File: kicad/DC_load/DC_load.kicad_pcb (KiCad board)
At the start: 2 copper layers, 110 x 145 mm, 190 parts, among them J1 BNC, J10 DC fan connector, J2 red_terminal, J3 red terminal, J4 black terminal, J5 black terminal, J6 USB_B, J8 FT232 programming port, J9 Conn_01x04_Socket, Q1 MMBT5401, Q13 AO3400A, Q3 FQP19N20C, Q4 FQP19N20C, Q5 FQP19N20C, Q6 FQP19N20C, SW1 RotaryEncoder_Switch, SW2 RotaryEncoder_Switch, SW3 SW_Push, SW8 SW_Push, U1 FSA3157P6X, U10 FSA3157P6X, U11 FSA3157P6X, U12 FSA3157P6X, U13 TLV9062, U14 AMS1117-3.3, U15 74HC14D653, U16 93LCxxB, U17 CH340C, U18 TL431DBZ, U2 Screen, U3 NCS21802, U4 NCS21802, U5 TLV9062, U6 TLV9062, U7 LMT84LPM, U8 STM32F103C8Tx, U9 Front plate

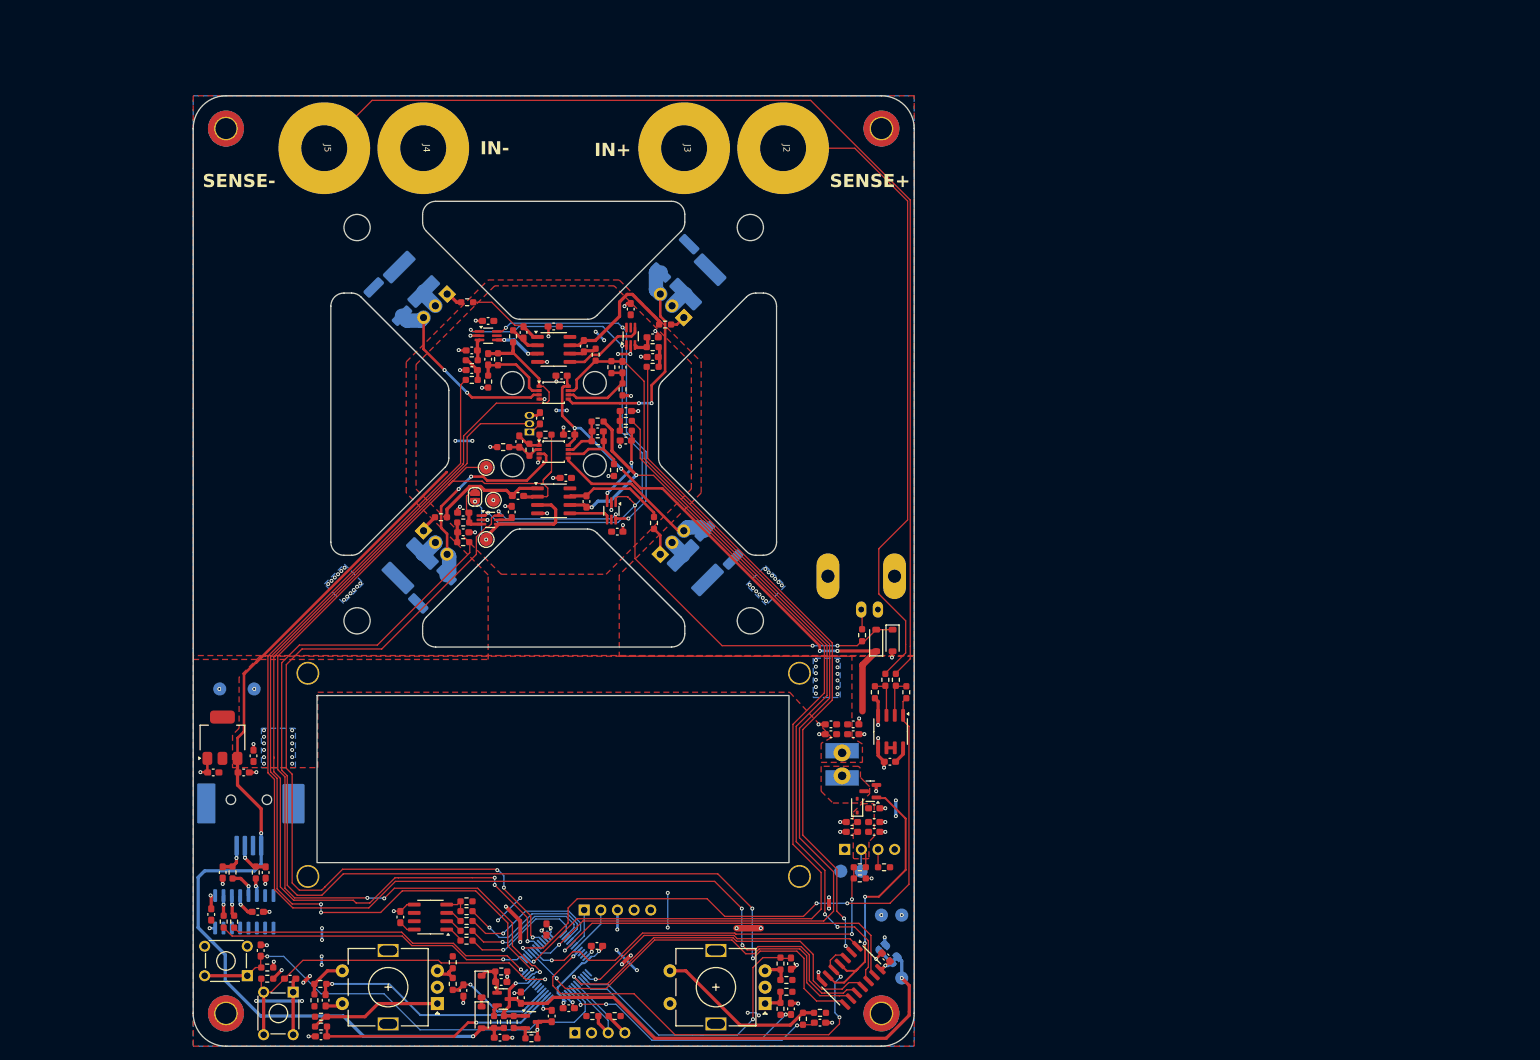
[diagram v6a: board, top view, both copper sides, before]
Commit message: Vbe multiplier, constant current source 12V mosfet gate driver. RC filters moved lower. INA181 for 20x gain, 50 mOhm shunts. Jumper moved to BNC. Rough placement initiated.
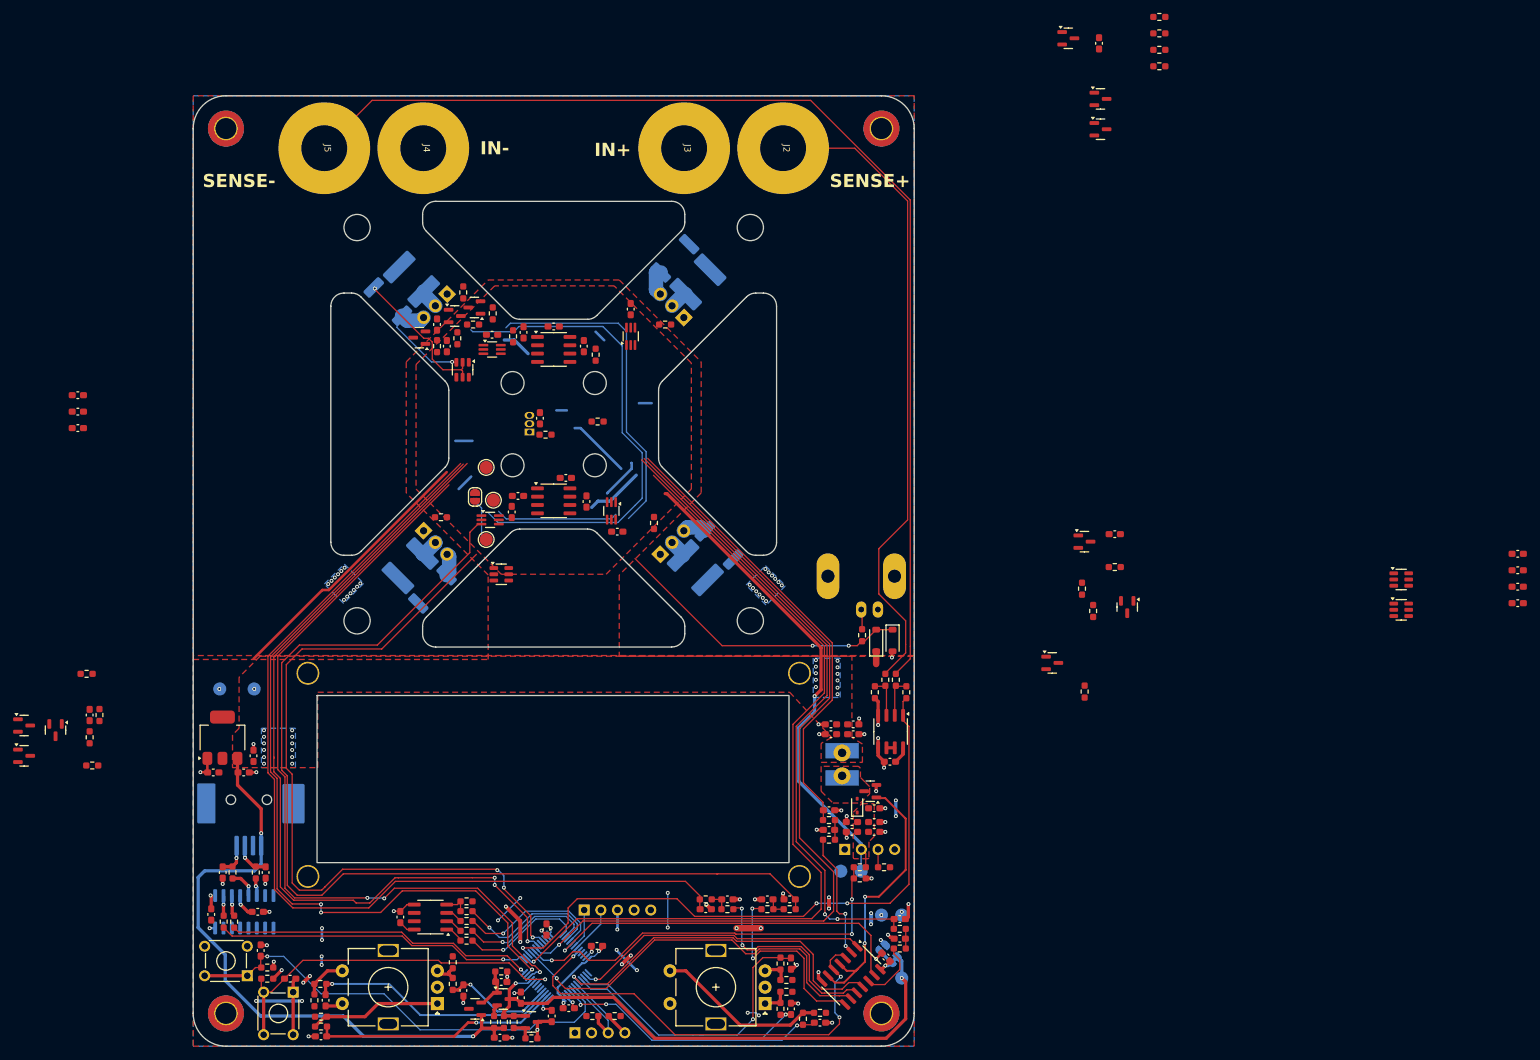
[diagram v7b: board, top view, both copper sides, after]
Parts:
- removed U3, U4: NCS21802, Package_SO:OnSemi_Micro8
- added C64: 100n, Capacitor_SMD:C_0603_1608Metric_Pad1.08x0.95mm_HandSolder, F.Cu at (252.1, 124.9)
- added C65: 100n, Capacitor_SMD:C_0603_1608Metric_Pad1.08x0.95mm_HandSolder, F.Cu at (252.1, 127.4)
- added C66: 100n, Capacitor_SMD:C_0603_1608Metric_Pad1.08x0.95mm_HandSolder, F.Cu at (88.7, 88.2)
- added C67: 100n, Capacitor_SMD:C_0603_1608Metric_Pad1.08x0.95mm_HandSolder, F.Cu at (32.4, 95.7)
- added C68: 100n, Capacitor_SMD:C_0603_1608Metric_Pad1.08x0.95mm_HandSolder, F.Cu at (32.4, 98.2)
- added C69: 100n, Capacitor_SMD:C_0603_1608Metric_Pad1.08x0.95mm_HandSolder, F.Cu at (32.4, 100.7)
- added D6: BAV99, Package_TO_SOT_SMD:SOT-23, F.Cu at (93.0, 189.3)
- added D7: BAV99, Package_TO_SOT_SMD:SOT-23, F.Cu at (84.5, 86.9)
- added D8: BAV99, Package_TO_SOT_SMD:SOT-23, F.Cu at (183.5, 41.2)
- added Q10: MMBT5401, Package_TO_SOT_SMD:SOT-23, F.Cu at (89.9, 83.6)
- added Q11: MMBT5551L, Package_TO_SOT_SMD:SOT-23, F.Cu at (92.9, 82.3)
- added Q12: MMBT5401, Package_TO_SOT_SMD:SOT-23, F.Cu at (188.4, 50.5)
- added Q14: MMBT5551L, Package_TO_SOT_SMD:SOT-23, F.Cu at (188.4, 55.1)
- added Q2: MMBT5401, Package_TO_SOT_SMD:SOT-23, F.Cu at (24.2, 146.1)
- added Q7: MMBT5551L, Package_TO_SOT_SMD:SOT-23, F.Cu at (24.2, 150.7)
- added Q8: MMBT5401, Package_TO_SOT_SMD:SOT-23, F.Cu at (181.1, 136.5)
- added Q9: MMBT5551L, Package_TO_SOT_SMD:SOT-23, F.Cu at (186.0, 118.0)
- added R67: 10k, Resistor_SMD:R_0603_1608Metric_Pad0.98x0.95mm_HandSolder, F.Cu at (87.2, 88.2)
- added R68: 10k, Resistor_SMD:R_0603_1608Metric_Pad0.98x0.95mm_HandSolder, F.Cu at (92.7, 84.9)
- added R69: 3k3, Resistor_SMD:R_0603_1608Metric_Pad0.98x0.95mm_HandSolder, F.Cu at (95.7, 83.2)
- added R70: 100, Resistor_SMD:R_0603_1608Metric_Pad0.98x0.95mm_HandSolder, F.Cu at (90.3, 87.0)
- added R71: 100, Resistor_SMD:R_0603_1608Metric_Pad0.98x0.95mm_HandSolder, F.Cu at (197.4, 38.0)
- added R72: 10k, Resistor_SMD:R_0603_1608Metric_Pad0.98x0.95mm_HandSolder, F.Cu at (197.4, 40.5)
- added R73: 3k3, Resistor_SMD:R_0603_1608Metric_Pad0.98x0.95mm_HandSolder, F.Cu at (197.4, 43.0)
- added R74: 10k, Resistor_SMD:R_0603_1608Metric_Pad0.98x0.95mm_HandSolder, F.Cu at (197.4, 45.5)
- added U19: INA181, Package_TO_SOT_SMD:SOT-23-6, F.Cu at (97.0, 123.0)
- added U20: INA181, Package_TO_SOT_SMD:SOT-23-6, F.Cu at (91.1, 91.8)
- added U21: INA181, Package_TO_SOT_SMD:SOT-23-6, F.Cu at (234.3, 123.8)
- added U22: INA181, Package_TO_SOT_SMD:SOT-23-6, F.Cu at (234.3, 128.4)
- C1, C2, C4, C7: value 100p -> 10u
- D3, D4: value 1N4148W -> BAV99; footprint Diode_SMD:D_SOD-123 -> Package_TO_SOT_SMD:SOT-23
- R1, R13, R16, R8: value 100 -> 10k
- R11, R18: value 10k -> 3k3
- R14, R15, R3, R9: value 10 mOhm -> 50 mOhm
- R31, R6: value 10k -> 100
- moved C46 148.9 mm to (252.1, 122.4)
- moved C9 145.9 mm to (252.1, 119.9)
- moved D4 116.7 mm to (192.5, 128.0)
- moved C24 92.4 mm to (128.2, 174.1), turned to 180 degrees
- moved C1 91.9 mm to (190.6, 116.9), turned to 0 degrees
- moved R11 91.6 mm to (34.6, 152.2)
- moved R31 91.1 mm to (190.6, 121.9), turned to 0 degrees
- moved C25 90.7 mm to (157.8, 178.6), turned to 180 degrees
- moved R25 90.7 mm to (157.8, 180.1), turned to 180 degrees
- moved C23 89.7 mm to (131.5, 172.6), turned to 0 degrees
- moved R23 89.7 mm to (131.5, 174.1), turned to 0 degrees
- moved R24 89.7 mm to (128.2, 172.6), turned to 0 degrees
- moved C7 87.9 mm to (188.2, 42.0)
- moved R26 86.7 mm to (157.8, 177.1), turned to 0 degrees
- moved C26 84.1 mm to (157.8, 175.6), turned to 180 degrees
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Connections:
- C1 pad 1: Net-(C1-Pad1) -> 12V
- C1 pad 2: Net-(U3A--) -> Net-(D4-A)
- C10 pad 2: 5V -> 3V3
- C11 pad 2: 5V -> 3V3
- C2 pad 1: /Microcontroller/CH2_MEAS -> 12V
- C2 pad 2: Net-(U4A--) -> Net-(D3-A)
- C20 pad 1: /Microcontroller/CH1_MEAS -> Net-(U5A--)
- C20 pad 2: Net-(C20-Pad2) -> Net-(Q7-E)
- C22 pad 2: Net-(JP3-A) -> Net-(C22-Pad2)
- C3 pad 2: Net-(C3-Pad2) -> Net-(Q11-E)
- C35 pad 1: Net-(D3-K) -> Net-(D6-A)
- C4 pad 1: Net-(C4-Pad1) -> 12V
- C4 pad 2: Net-(U3B--) -> Net-(D7-A)
- C5 pad 1: /Microcontroller/CH3_MEAS -> Net-(U5B--)
- C5 pad 2: Net-(C5-Pad2) -> Net-(Q9-E)
- C54 pad 1: /Microcontroller/FAN_OUT -> 12V
- C55 pad 1: /Microcontroller/FAN_OUT -> 12V
- C6 pad 2: Net-(C6-Pad2) -> Net-(Q14-E)
- C61 pad 1: /Microcontroller/FAN_OUT -> 12V
- C62 pad 1: /Microcontroller/FAN_OUT -> 12V
- C63 pad 1: /Microcontroller/FAN_OUT -> 12V
- C7 pad 1: /Microcontroller/CH4_MEAS -> 12V
- C7 pad 2: Net-(U4B--) -> Net-(D8-A)
- C8 pad 1: 5V -> 3V3
- D3 pad 1: Net-(D3-K) -> 12V
- D4 pad 1: Net-(D3-A) -> 12V
- D4 pad 2: 5V -> Net-(D4-A)
- D5 pad 1: /Microcontroller/FAN_OUT -> 12V
- J10 pad 2: /Microcontroller/FAN_OUT -> 12V
- J10 pad 4: unconnected-(J10-Pin_4-Pad4) -> FAN_PWM
- JP3 pad 1: Net-(JP3-A) -> /Microcontroller/BNC_CONTROL
- Q1 pad 1: Net-(D3-K) -> Net-(D6-A)
- R1 pad 1: GND -> Net-(D3-A)
- R1 pad 2: Net-(U3A--) -> GND
- R10 pad 1: Net-(C4-Pad1) -> /Microcontroller/CH3_MEAS
- R10 pad 2: /Microcontroller/CH3_MEAS -> Net-(U5B--)
- R11 pad 1: Net-(U3B--) -> Net-(Q7-B)
- R11 pad 2: Net-(C4-Pad1) -> Net-(Q7-E)
- R12 pad 2: Net-(C5-Pad2) -> Net-(Q8-C)
- R13 pad 1: GND -> Net-(D4-A)
- R13 pad 2: Net-(U3B--) -> GND
- R16 pad 1: GND -> Net-(Q8-C)
- R16 pad 2: Net-(U4B--) -> Net-(Q9-B)
- R17 pad 2: Net-(C6-Pad2) -> Net-(Q12-C)
- R18 pad 1: Net-(U4B--) -> Net-(Q9-B)
- R18 pad 2: /Microcontroller/CH4_MEAS -> Net-(Q9-E)
- R2 pad 2: Net-(C20-Pad2) -> Net-(Q2-C)
- R21 pad 1: Net-(JP3-A) -> Net-(C22-Pad2)
- R31 pad 1: Net-(U3A--) -> Net-(Q8-E)
- R31 pad 2: Net-(C1-Pad1) -> 12V
- R4 pad 1: Net-(C1-Pad1) -> /Microcontroller/CH1_MEAS
- R4 pad 2: /Microcontroller/CH1_MEAS -> Net-(U5A--)
- R58 pad 1: Net-(D3-K) -> Net-(D6-A)
- R6 pad 1: Net-(U4A--) -> Net-(Q2-E)
- R6 pad 2: /Microcontroller/CH2_MEAS -> 12V
- R66 pad 1: /Microcontroller/FAN_OUT -> 12V
- R7 pad 2: Net-(C3-Pad2) -> Net-(Q10-C)
- R8 pad 1: GND -> Net-(Q2-C)
- R8 pad 2: Net-(U4A--) -> Net-(Q7-B)
- TP6 pad 1: /Microcontroller/FAN_OUT -> 12V
- TP9 pad 1: /Microcontroller/CH1_MEAS -> Net-(U5A--)
- U1 pad 3: Net-(JP3-A) -> Net-(C22-Pad2)
- U5 pad 1: Net-(C20-Pad2) -> Net-(Q7-E)
- U5 pad 2: /Microcontroller/CH1_MEAS -> Net-(U5A--)
- U5 pad 6: /Microcontroller/CH3_MEAS -> Net-(U5B--)
- U5 pad 7: Net-(C5-Pad2) -> Net-(Q9-E)
- U5 pad 8: 5V -> 3V3
- U6 pad 1: Net-(C3-Pad2) -> Net-(Q11-E)
- U6 pad 7: Net-(C6-Pad2) -> Net-(Q14-E)
- U6 pad 8: 5V -> 3V3
- U7 pad 1: 5V -> 3V3
- U8 pad 37: unconnected-(U8-PA14-Pad37) -> FAN_PWM
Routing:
- net Net-(R23-Pad2): track 195.8 -> 30.6 mm
- net Net-(C22-Pad2): track 0.00 -> 157.7 mm
- net Net-(R22-Pad2): track 175.0 -> 29.8 mm
- net Net-(C24-Pad2): track 3.25 -> 147.9 mm
- net Net-(R25-Pad2): track 106.3 -> 8.73 mm, vias 2 -> 0
- net Net-(C26-Pad2): track 12.6 -> 103.6 mm
- net Net-(R27-Pad2): track 105.9 -> 19.4 mm
- net 12V: track 0.00 -> 76.0 mm, vias 0 -> 1
- net Net-(C28-Pad2): track 3.63 -> 70.2 mm
- net 5V: track 160.9 -> 102.7 mm, vias 33 -> 26
- net /Microcontroller/CH1_MEAS: track 158.8 -> 122.5 mm, vias 4 -> 3
- net /Microcontroller/CH2_MEAS: track 163.2 -> 128.1 mm
- net Net-(Q6-S): track 35.1 -> 6.24 mm, vias 2 -> 0
- net 3V3: track 141.8 -> 113.0 mm, vias 29 -> 27
- net /Microcontroller/CH4_MEAS: track 160.5 -> 133.2 mm
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- added copper zone on F.Cu, net 12V
- removed copper zone on F.Cu, net /Microcontroller/FAN_OUT
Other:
- board text removed: "5V"
- board text removed: "GND"
